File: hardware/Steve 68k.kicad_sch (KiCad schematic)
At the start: 50 parts, among them IC1 MC68008FN12F, J1 Serial 1, J2 Conn_02x32_Odd_Even, J3 Conn_01x03_Male, J4 Conn_01x02_Male, J5 Conn_01x10, J6 Conn_01x10, J7 Serial 2, SW1 Reset, U1 74LS32, U2 SST39SF040, U3 74LS257, U4 74HC04, U5 MC68681FN, U6 74LS138, U7 AS6C4008-55PCN, U8 Max705, X1 4.0Mhz, X2 1.8432 Mhz

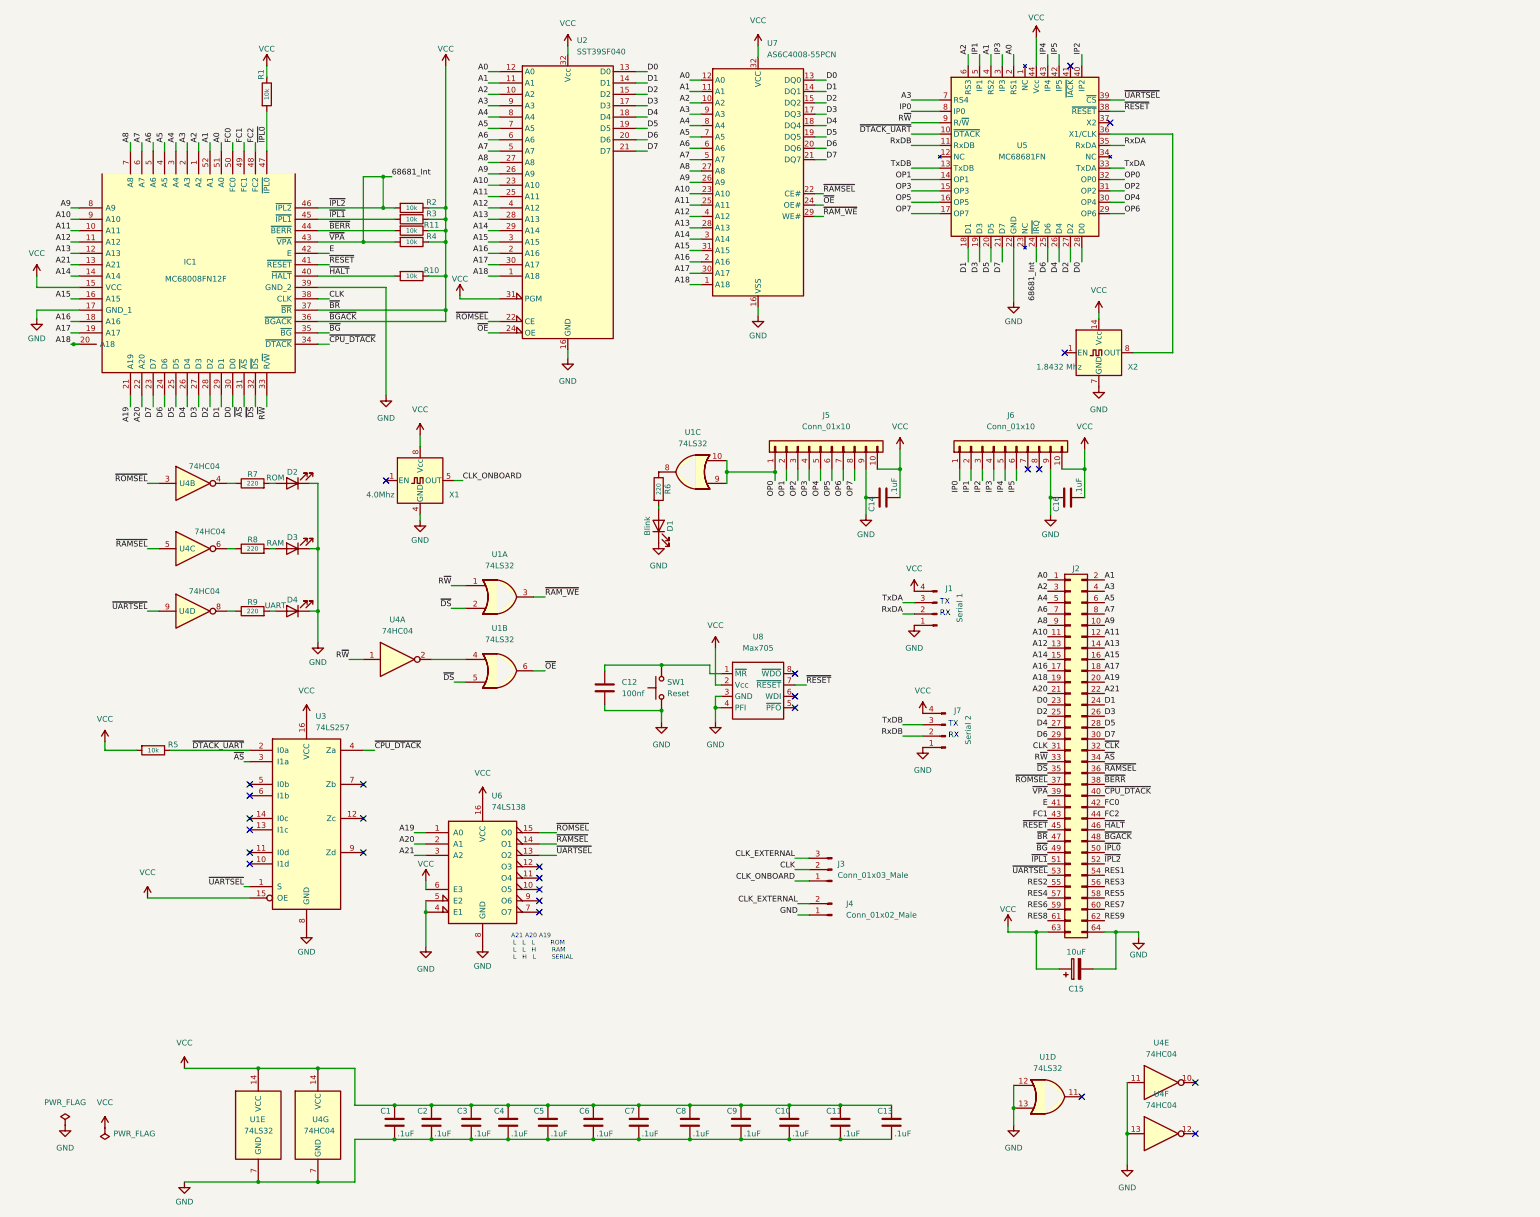
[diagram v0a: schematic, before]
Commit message: Fixed Dtack select
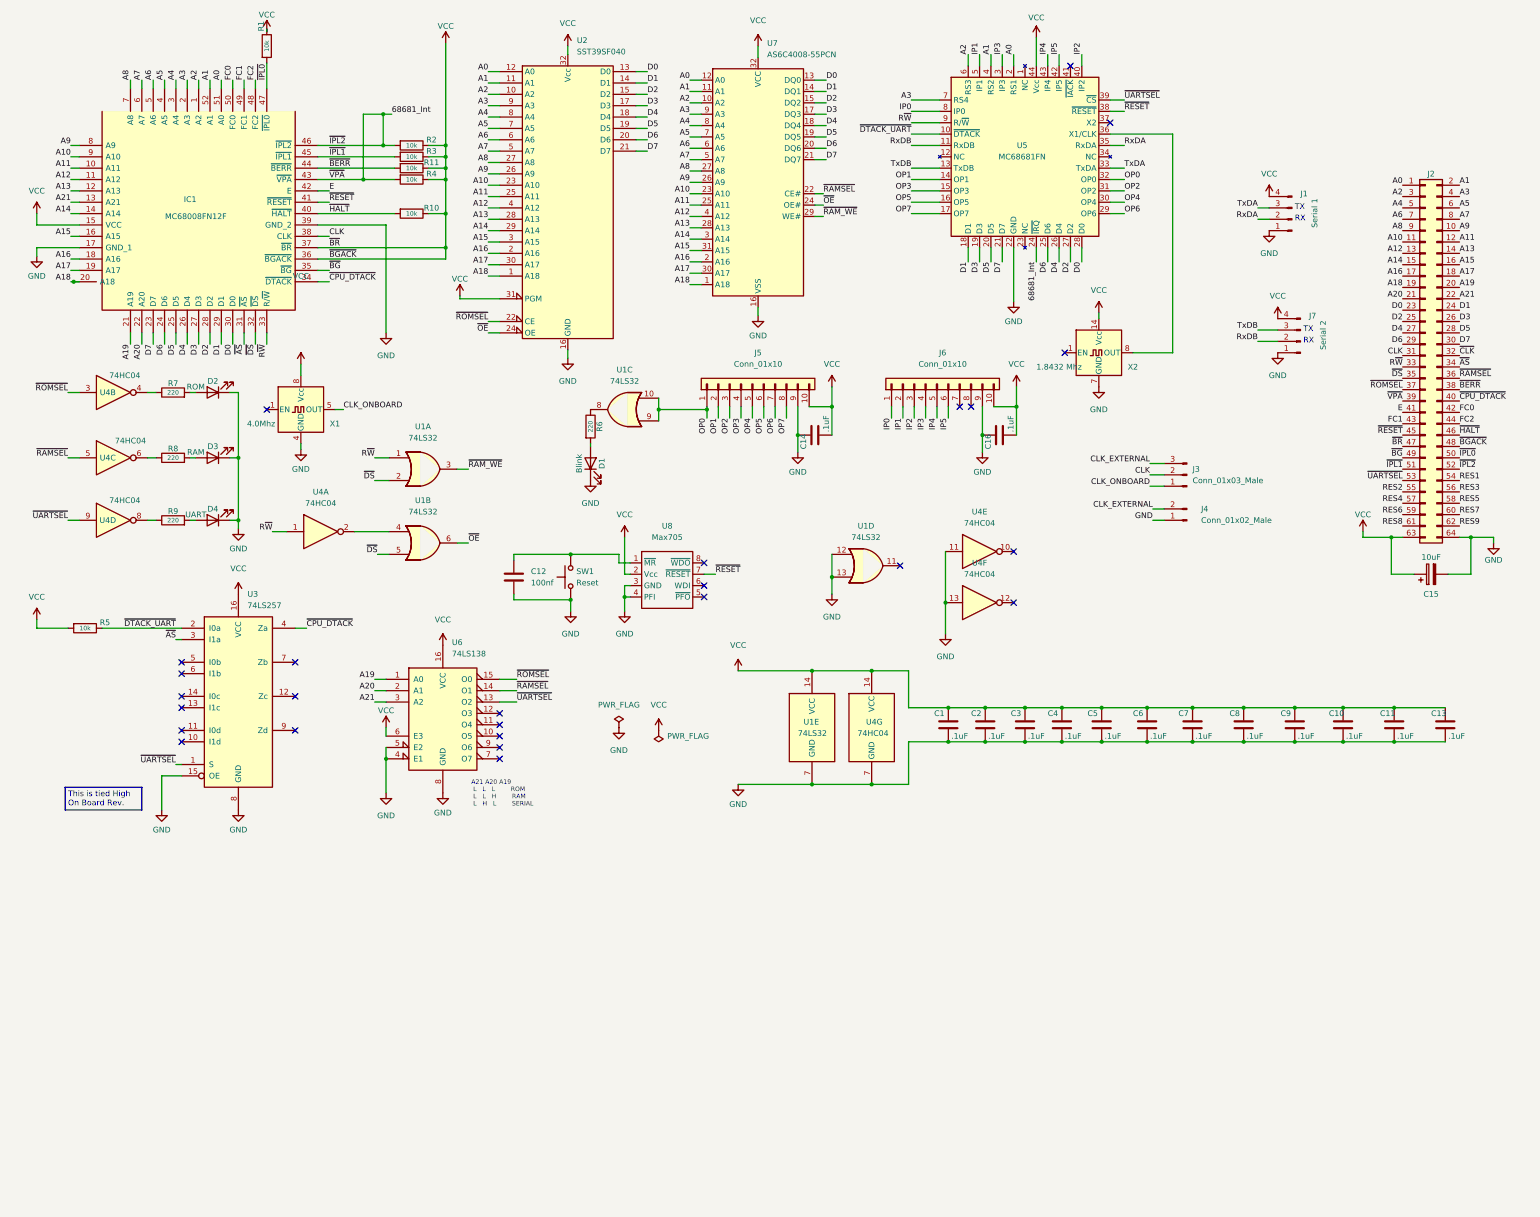
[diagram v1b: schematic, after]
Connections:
- net GND: now also U3.15 (OE)
- net VCC: no longer U3.15 (OE)
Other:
- note added: "This is tied High On Board Rev."
- moved on the sheet: C1, C10, C11, C12, C13, C14, C15, C16, C2, C3, C4, C5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

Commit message: Serial Test and some changes to the PCB
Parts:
- removed C13: .1uF, Capacitor_SMD:C_0603_1608Metric, symbol Device:C
- removed IC1: MC68008FN12F, Package_LCC:PLCC-52_THT-Socket, symbol mc68k:MC68008FN12F
- removed U2: SST39SF040, Package_LCC:PLCC-32_THT-Socket, symbol mc68k:SST39SF040
- removed X1: 4.0Mhz, Oscillator:Oscillator_DIP-8, symbol Oscillator:CXO_DIP14
- added IC1: MC68008FN8, Package_LCC:PLCC-52_THT-Socket, symbol mc68k:MC68008FN8
- added R12, R13: 10k, Resistor_SMD:R_0603_1608Metric, symbol Device:R
- added U2: 28C256, Package_DIP:DIP-28_W15.24mm_Socket_LongPads, symbol Memory_EEPROM:28C256
- added X1: CXO_DIP8, Oscillator:Oscillator_DIP-8, symbol mc68k:CXO_DIP8
- SW1: footprint Button_Switch_SMD:SW_Push_1P1T_NO_6x6mm_H9.5mm -> Button_Switch_THT:SW_PUSH_6mm
- U1, U4: footprint Package_DIP:DIP-14_W7.62mm_Socket_LongPads -> Package_SO:SOIC-14_3.9x8.7mm_P1.27mm
- U6: footprint Package_DIP:DIP-16_W7.62mm_Socket_LongPads -> Package_SO:SOIC-16_3.9x9.9mm_P1.27mm
- U7: footprint Package_DIP:DIP-32_W15.24mm_Socket_LongPads -> Package_SO:SSOP-32_11.305x20.495mm_P1.27mm
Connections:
- net 68681_Int: now also IC1.43 (~{VPA}), IC1.46 (~{IPL2})
- net A0: now also IC1.51 (A0), U2.10 (A0)
- net A1: now also IC1.52 (A1), U2.9 (A1)
- net A10: now also IC1.9 (A10), U2.21 (A10)
- net A11: now also IC1.10 (A11), U2.23 (A11)
- net A12: now also IC1.11 (A12), U2.2 (A12)
- net A13: now also IC1.12 (A13), U2.26 (A13)
- net A14: now also IC1.14 (A14), U2.1 (A14)
- net A15: now also IC1.16 (A15)
- net A16: now also IC1.18 (A16)
- net A17: now also IC1.19 (A17)
- net A18: now also IC1.20 (A18)
- net A19: now also IC1.21 (A19)
- net A2: now also IC1.1 (A2), U2.8 (A2)
- net A20: now also IC1.22 (A20)
- net A21: now also IC1.13 (A21)
- net A3: now also IC1.2 (A3), U2.7 (A3)
- net A4: now also IC1.3 (A4), U2.6 (A4)
- net A5: now also IC1.4 (A5), U2.5 (A5)
- net A6: now also IC1.5 (A6), U2.4 (A6)
- net A7: now also IC1.6 (A7), U2.3 (A7)
- net A8: now also IC1.7 (A8), U2.25 (A8)
- net A9: now also IC1.8 (A9), U2.24 (A9)
- net CLK: now also IC1.38 (CLK)
- net CLK_ONBOARD: now also X1.5 (OUT)
- net D0: now also IC1.30 (D0), U2.11 (D0)
- net D1: now also IC1.29 (D1), U2.12 (D1)
- net D2: now also IC1.28 (D2), U2.13 (D2)
- net D3: now also IC1.27 (D3), U2.15 (D3)
- net D4: now also IC1.26 (D4), U2.16 (D4)
- net D5: now also IC1.25 (D5), U2.17 (D5)
- net D6: now also IC1.24 (D6), U2.18 (D6)
- net D7: now also IC1.23 (D7), U2.19 (D7)
- net E: now also IC1.42 (E)
- net FC0: now also IC1.50 (FC0)
- net FC1: now also IC1.49 (FC1)
- net FC2: now also IC1.48 (FC2)
- net GND: now also IC1.17 (GND_1), IC1.39 (GND_2), U2.14 (GND), X1.4 (GND)
- net R~{W}: now also IC1.33 (R/~{W})
- net VCC: now also IC1.15 (VCC), R12.1, R13.1, U2.27 (~{WE}), U2.28 (VCC), X1.8 (Vcc); no longer J2.47 (Pin_47), J2.48 (Pin_48)
- net ~{AS}: now also IC1.31 (~{AS})
- net ~{BERR}: now also IC1.44 (~{BERR})
- net ~{BG}: now also IC1.35 (~{BG})
- net ~{CPU_DTACK}: now also IC1.34 (~{DTACK})
- net ~{DS}: now also IC1.32 (~{DS})
- net ~{HALT}: now also IC1.40 (~{HALT})
- net ~{IPL0}: now also IC1.47 (~{IPL0})
- net ~{IPL1}: now also IC1.45 (~{IPL1})
- net ~{OE}: now also U2.22 (~{OE})
- net ~{RESET}: now also IC1.41 (~{RESET})
- net ~{ROMSEL}: now also U2.20 (~{CS})
- net UART_CLK: now reaches U5.36 (X1/CLK), X2.8 (OUT)
- new net ~{BGACK}: IC1.36 (~{BGACK}), J2.48 (Pin_48), R13.2
- new net ~{BR}: IC1.37 (~{BR}), J2.47 (Pin_47), R12.2
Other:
- note added: "A21 A20 A19 L L L ROM L L H RAM L H L SERIAL H L L I2C"
- note removed: "A21 A20 A19 L L L ROM L L H RAM L H L SERIAL"
- note removed: "This is tied High On Board Rev."
- moved on the sheet: C12, C14, C15, C16, D1, D2, D3, D4, J1, J2, J3, J4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

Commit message: Misc
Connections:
- net RES1 is gone; now on net ~{SEL1}: J2.54 (Pin_54)
- net RES2 is gone; now on net ~{SEL2}: J2.55 (Pin_55)
- net RES3 is gone; now on net ~{SEL3}: J2.56 (Pin_56)
- net RES4 is gone; now on net ~{SEL4}: J2.57 (Pin_57)
- net RES5 is gone; now on net ~{SEL5}: J2.58 (Pin_58)
- net ~{SEL3}: now reaches U6.10 (O5)
- net ~{SEL2}: now reaches U6.11 (O4)
- net ~{SEL1}: now reaches U6.12 (O3)
- net ~{SEL5}: now reaches U6.7 (O7)
- net ~{SEL4}: now reaches U6.9 (O6)
- no-connect marks 26 -> 21
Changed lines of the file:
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@@
   (junction (at 62.23 225.425) (diameter 0) (color 0 0 0 0)
   )
-  (no_connect (at 132.715 255.27))
-  (no_connect (at 132.715 250.19))
-  (no_connect (at 132.715 252.73))
-  (no_connect (at 132.715 245.11))
-  (no_connect (at 132.715 247.65))
   (no_connect (at 180.34 232.41))
   (no_connect (at 38.1 114.935))
@@
     (stroke (width 0) (type default) (color 0 0 0 0))
   )
+  (wire (pts (xy 132.715 247.65) (xy 136.525 247.65))
+    (stroke (width 0) (type default) (color 0 0 0 0))
+  )
   (wire (pts (xy 395.605 107.315) (xy 395.605 99.06))
     (stroke (width 0) (type default) (color 0 0 0 0))
@@
     (stroke (width 0) (type default) (color 0 0 0 0))
   )
+  (wire (pts (xy 132.715 245.11) (xy 136.525 245.11))
+    (stroke (width 0) (type default) (color 0 0 0 0))
+  )
   (wire (pts (xy 332.105 26.67) (xy 338.455 26.67))
     (stroke (width 0) (type default) (color 0 0 0 0))
@@
     (stroke (width 0) (type default) (color 0 0 0 0))
   )
+  (wire (pts (xy 132.715 252.73) (xy 136.525 252.73))
+    (stroke (width 0) (type default) (color 0 0 0 0))
+  )
   (wire (pts (xy 302.26 43.815) (xy 305.435 43.815))
     (stroke (width 0) (type default) (color 0 0 0 0))
@@
     (stroke (width 0) (type default) (color 0 0 0 0))
   )
+  (wire (pts (xy 132.715 250.19) (xy 136.525 250.19))
+    (stroke (width 0) (type default) (color 0 0 0 0))
+  )
   (wire (pts (xy 160.655 69.215) (xy 152.4 69.215))
     (stroke (width 0) (type default) (color 0 0 0 0))
@@
   )
   (wire (pts (xy 91.44 43.815) (xy 91.44 39.37))
+    (stroke (width 0) (type default) (color 0 0 0 0))
+  )
+  (wire (pts (xy 132.715 255.27) (xy 136.525 255.27))
     (stroke (width 0) (type default) (color 0 0 0 0))
   )
@@
     (effects (font (size 1.27 1.27)) (justify right bottom))
   )
+  (label "~{SEL2}" (at 136.525 247.65 0)
+    (effects (font (size 1.27 1.27)) (justify left bottom))
+  )
   (label "D1" (at 180.975 31.115 0)
     (effects (font (size 1.27 1.27)) (justify left bottom))
@@
     (effects (font (size 1.27 1.27)) (justify right bottom))
   )
+  (label "~{SEL1}" (at 136.525 245.11 0)
+    (effects (font (size 1.27 1.27)) (justify left bottom))
+  )
   (label "IP1" (at 273.05 23.495 90)
     (effects (font (size 1.27 1.27)) (justify left bottom))
@@
     (effects (font (size 1.27 1.27)) (justify left bottom))
   )
+  (label "~{SEL3}" (at 136.525 250.19 0)
+    (effects (font (size 1.27 1.27)) (justify left bottom))
+  )
   (label "A2" (at 55.88 30.48 90)
     (effects (font (size 1.27 1.27)) (justify left bottom))
@@
     (effects (font (size 1.27 1.27)) (justify right bottom))
   )
-  (label "RES5" (at 393.065 91.44 0)
+  (label "~{SEL5}" (at 393.065 91.44 0)
     (effects (font (size 1.27 1.27)) (justify left bottom))
   )
@@
     (effects (font (size 1.27 1.27)) (justify right bottom))
   )
-  (label "RES2" (at 380.365 88.9 180)
+  (label "~{SEL2}" (at 380.365 88.9 180)
     (effects (font (size 1.27 1.27)) (justify right bottom))
   )
@@
     (effects (font (size 1.27 1.27)) (justify left bottom))
   )
+  (label "~{SEL4}" (at 136.525 252.73 0)
+    (effects (font (size 1.27 1.27)) (justify left bottom))
+  )
   (label "D4" (at 380.365 53.34 180)
     (effects (font (size 1.27 1.27)) (justify right bottom))
@@
     (effects (font (size 1.27 1.27)) (justify right bottom))
   )
-  (label "RES1" (at 393.065 86.36 0)
+  (label "~{SEL1}" (at 393.065 86.36 0)
     (effects (font (size 1.27 1.27)) (justify left bottom))
   )
@@
     (effects (font (size 1.27 1.27)) (justify right bottom))
   )
-  (label "RES3" (at 393.065 88.9 0)
+  (label "~{SEL3}" (at 393.065 88.9 0)
     (effects (font (size 1.27 1.27)) (justify left bottom))
   )
@@
     (effects (font (size 1.27 1.27)) (justify left bottom))
   )
+  (label "~{SEL5}" (at 136.525 255.27 0)
+    (effects (font (size 1.27 1.27)) (justify left bottom))
+  )
   (label "R~{W}" (at 257.81 38.735 180)
     (effects (font (size 1.27 1.27)) (justify right bottom))
@@
     (effects (font (size 1.27 1.27)) (justify left bottom))
   )
-  (label "RES4" (at 380.365 91.44 180)
-    (effects (font (size 1.27 1.27)) (justify right bottom))
-  )
+  (label "~{SEL4}" (at 380.365 91.44 180)
+    (effects (font (size 1.27 1.27)) (justify right bottom))
+  )

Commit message: Working on PLD for Glue Logic
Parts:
- added C13: .1uF, Capacitor_SMD:C_0603_1608Metric, symbol Device:C
- added C17, C18: 22pf, Capacitor_SMD:C_0603_1608Metric, symbol Device:C
- added U9: ATmega328-P, Package_DIP:DIP-28_W7.62mm, symbol MCU_Microchip_ATmega:ATmega328-P
- added U?: 74LS253, symbol 74xx:74LS253
- added Y1: Crystal, symbol Device:Crystal
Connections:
- net A0: now also U9.5 (PD3)
- net A1: now also U9.6 (PD4)
- net A2: now also U9.25 (PC2)
- net A3: now also U9.26 (PC3)
- net CLK: now also U9.4 (PD2)
- net D0: now also U9.14 (PB0)
- net D1: now also U9.15 (PB1)
- net D2: now also U9.16 (PB2)
- net D3: now also U9.17 (PB3)
- net D4: now also U9.18 (PB4)
- net D5: now also U9.19 (PB5)
- net D6: now also U9.12 (PD6)
- net D7: now also U9.13 (PD7)
- net GND: now also C13.2, C17.2, C18.2, U9.22 (GND), U9.8 (GND), U?.1 (OEa), U?.8 (GND)
- net R~{W}: now also U9.24 (PC1)
- net VCC: now also C13.1, U9.7 (VCC), U?.15 (OEb), U?.16 (VCC)
- net ~{AS}: now also U?.6 (I0a)
- net ~{CPU_DTACK}: now also U?.7 (Za)
- net ~{RESET}: now also U9.1 (~{RESET}/PC6)
- net ~{UARTSEL}: now also U?.14 (A0)
- net ~{SEL1} renamed ~{I2CSEL}
- net ~{I2CSEL}: now also U?.2 (A1)
- new net: C17.1, U9.9 (XTAL1/PB6), Y1.1
- new net: C18.1, U9.10 (XTAL2/PB7), Y1.2
- new net RxD: U9.2 (PD0)
- new net SCLK: U9.28 (PC5)
- new net SDA: U9.27 (PC4)
- new net TxD: U9.3 (PD1)
- new net ~DTACK_I2C: U?.4 (I2a)
- new net ~DTACK_UART: U?.5 (I1a)
- new net ~DTACK_USER: U?.3 (I3a)
- new net ~{CE}: U9.23 (PC0)
- no-connect marks 21 -> 29
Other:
- note added: "A21 A20 A19 L L L ROM L L H RAM L H L SERIAL L H H I2C"
- note removed: "A21 A20 A19 L L L ROM L L H RAM L H L SERIAL H L L I2C"
- moved on the sheet: C12, C4, SW1, U1A, U1B, U4A, U8

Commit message: New version of PCB using a GAL
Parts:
- removed C13, C14, C16, C5: .1uF, Capacitor_SMD:C_0603_1608Metric, symbol Device:C
- removed C17, C18: 22pf, Capacitor_SMD:C_0603_1608Metric, symbol Device:C
- removed J4: Conn_01x02_Male, Connector_PinHeader_2.54mm:PinHeader_1x02_P2.54mm_Vertical, symbol Connector:Conn_01x02_Male
- removed J5, J6: Conn_01x10, Connector_PinHeader_2.54mm:PinHeader_1x10_P2.54mm_Vertical, symbol Connector_Generic:Conn_01x10
- removed U3: 74LS257, Package_DIP:DIP-16_W7.62mm_Socket_LongPads, symbol 74xx:74LS257
- removed U6: 74LS138, Package_SO:SOIC-16_3.9x9.9mm_P1.27mm, symbol 74xx:74LS138
- removed U9: ATmega328-P, Package_DIP:DIP-28_W7.62mm, symbol MCU_Microchip_ATmega:ATmega328-P
- removed U?: 74LS253, symbol 74xx:74LS253
- removed Y1: Crystal, symbol Device:Crystal
- added D5: USER, LED_SMD:LED_1206_3216Metric, symbol Device:LED
- added U3: GAL16V8, Package_DIP:DIP-20_W7.62mm_Socket_LongPads, symbol Logic_Programmable:GAL16V8
- D1: value Blink -> I2C
- R5: value 10k -> 220
- renumbered J2 to J1, J1 to J2, J7 to J3, J3 to J4
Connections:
- net ~{CLK} is gone; now on net CLK_EXTERNAL: J1.32 (Pin_32)
- net A19: now also U3.2 (I2)
- net A20: now also U3.3 (I3)
- net A21: now also U3.4 (I4)
- net CLK: now also U3.1 (I1/CLK)
- net GND: now also U1.10, U1.9, D5.1 (K), U3.10 (GND), U3.11 (I10/~{OE}); no longer U4.11, U4.13
- net OP0: no longer U1.10, U1.9
- net VCC: now also U3.20 (VCC); no longer R5.2
- net ~{AS}: now also U3.5 (I5)
- net ~{DTACK_UART}: now also U3.6 (I6); no longer R5.1
- net ~{I2CSEL}: now also U4.11, U3.15 (IO5)
- net ~{RAMSEL}: now also U3.13 (IO7)
- net ~{ROMSEL}: now also U3.12 (IO8)
- net ~{UARTSEL}: now also U3.14 (IO6)
- net at R6.1: now also U4.12; no longer U1.8
- net at U4.10: now also R5.1
- net at R6.2: now also D5.2 (A); no longer D1.2 (A)
- net RES6: no longer names the net of J1.59 (Pin_59)
- net RES7: no longer names the net of J1.60 (Pin_60)
- net RES8: no longer names the net of J1.61 (Pin_61)
- net RES9: no longer names the net of J1.62 (Pin_62)
- net ~{CPU_DTACK} renamed ~{DTACK_CPU}
- net ~{DTACK_CPU}: now also U3.16 (IO4)
- net ~{SEL2} renamed ~{USERSEL}
- net ~{USERSEL}: now also U4.13, U3.9 (I9)
- net ~{SEL3} renamed ~{DTACK_USER}
- net ~{DTACK_USER}: now also U3.8 (I8)
- net ~{SEL4}: no longer names the net of J1.57 (Pin_57)
- net ~{SEL5}: no longer names the net of J1.58 (Pin_58)
- new net: D1.2 (A), R5.2
- new net DTACK_I2C: U3.7 (I7)
- no-connect marks 29 -> 18
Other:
- note added: "Glue Logic"
- note added: "Reset"
- note removed: "A21 A20 A19 L L L ROM L L H RAM L H L SERIAL L H H I2C"
- moved on the sheet: C10, C11, U1D, U1E, U4G

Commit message: More GAL and glue logic stuff
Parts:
- added C13, C5: .1uF, Capacitor_SMD:C_0603_1608Metric, symbol Device:C
- added J5: I2C, symbol Connector:Conn_01x04_Male
- added R14: 10k, symbol Device:R
- added U10, U6: 74HC04, symbol 74xx:74HC04
- added U9: PCA9564, symbol mc68k:PCA9564
- J4: value Conn_01x03_Male -> CLK Select
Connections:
- net A0: now also U9.14 (A0)
- net A1: now also U9.15 (A1)
- net D0: now also U9.1 (D0)
- net D1: now also U9.2 (D1)
- net D2: now also U9.3 (D2)
- net D3: now also U9.4 (D3)
- net D4: now also U9.5 (D4)
- net D5: now also U9.6 (D5)
- net D6: now also U9.7 (D6)
- net D7: now also U9.8 (D7)
- net GND: now also C13.2, C5.2, J5.1 (Pin_1), U10.7 (GND), U6.11, U6.13, U6.5, U6.9, U9.10 (Gnd)
- net R~{W}: now also U6.1, U9.11 (~{WD})
- net VCC: now also C13.1, C5.1, J5.4 (Pin_4), R14.1, U10.14 (VCC), U9.20 (Vcc)
- net ~{I2CSEL}: now also U9.13 (~{CE})
- net ~{RESET}: now also U9.17 (~{RESET})
- new net: U6.2, U9.12 (~{RD})
- new net: R14.2, U9.16 (~{INT})
- new net SCA: J5.3 (Pin_3)
- new net SDl: J5.2 (Pin_2)
- no-connect marks 18 -> 23
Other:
- moved on the sheet: D1, D2, D3, D4, D5, J2, J3, J4, R5, R6, R7, R8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
